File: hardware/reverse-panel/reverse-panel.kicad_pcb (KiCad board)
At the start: 2 copper layers, 116 x 102 mm, 328 parts, among them J1 Conn_01x03, U1 WCH CH32V003F4U6

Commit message: cleanup fab files
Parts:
- removed the R2 at (32.4, 50.0)
- removed the R2 at (84.4, 50.0)
- removed the R2 at (84.4, 102.0)
- removed the R2 at (32.4, 102.0)
- removed the R7 at (67.6, 50.0)
- removed the R7 at (119.6, 102.0)
- removed the R7 at (67.6, 102.0)
- removed the R7 at (119.6, 50.0)
- removed the align-r1 at (27.8, 104.4)
- removed the align-r1 at (79.8, 52.4)
- removed the align-r1 at (27.8, 52.4)
- removed the align-r1 at (79.8, 104.4)
- added R2: 47R, Resistor_SMD:R_0402_1005Metric, F.Cu at (84.4, 58.4)
- added R2: 47R, Resistor_SMD:R_0402_1005Metric, F.Cu at (32.4, 58.4)
- added R2: 47R, Resistor_SMD:R_0402_1005Metric, F.Cu at (32.4, 110.4)
- added R2: 47R, Resistor_SMD:R_0402_1005Metric, F.Cu at (84.4, 110.4)
- added R7: 47R, Resistor_SMD:R_0402_1005Metric, F.Cu at (67.6, 58.4)
- added R7: 47R, Resistor_SMD:R_0402_1005Metric, F.Cu at (119.6, 110.4)
- added R7: 47R, Resistor_SMD:R_0402_1005Metric, F.Cu at (119.6, 58.4)
- added R7: 47R, Resistor_SMD:R_0402_1005Metric, F.Cu at (67.6, 110.4)
- added align-r1: , , F.Cu at (79.8, 47.3)
- added align-r1: , , F.Cu at (79.8, 99.3)
- added align-r1: , , F.Cu at (27.8, 47.3)
- added align-r1: , , F.Cu at (27.8, 99.3)
- added align-r3: , , F.Cu at (27.8, 52.4)
- added align-r3: , , F.Cu at (79.8, 104.4)
- added align-r3: , , F.Cu at (27.8, 104.4)
- added align-r3: , , F.Cu at (79.8, 52.4)
- added align-r4: , , F.Cu at (72.2, 104.4)
- added align-r4: , , F.Cu at (124.2, 52.4)
- added align-r4: , , F.Cu at (72.2, 52.4)
- added align-r4: , , F.Cu at (124.2, 104.4)
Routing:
- net GND: track 17.1 -> 75.8 mm, vias 476 -> 424
- net /touch2: track 34.8 -> 66.6 mm
- net GP7: track 154.5 -> 139.2 mm
- net PWM2: track 65.3 -> 79.1 mm
- net PWM7: track 66.1 -> 80.0 mm
- net GP2: track 153.2 -> 140.5 mm
- net /touch1: track 68.9 -> 71.7 mm, vias 4 -> 12
- net Net-(D3-A): track 53.8 -> 52.0 mm
- net Net-(D13-A): track 53.2 -> 52.0 mm
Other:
- board size 116 x 102 mm -> 116.1 x 102.1 mm
- board text removed: "import QR SVG scale 0.2"

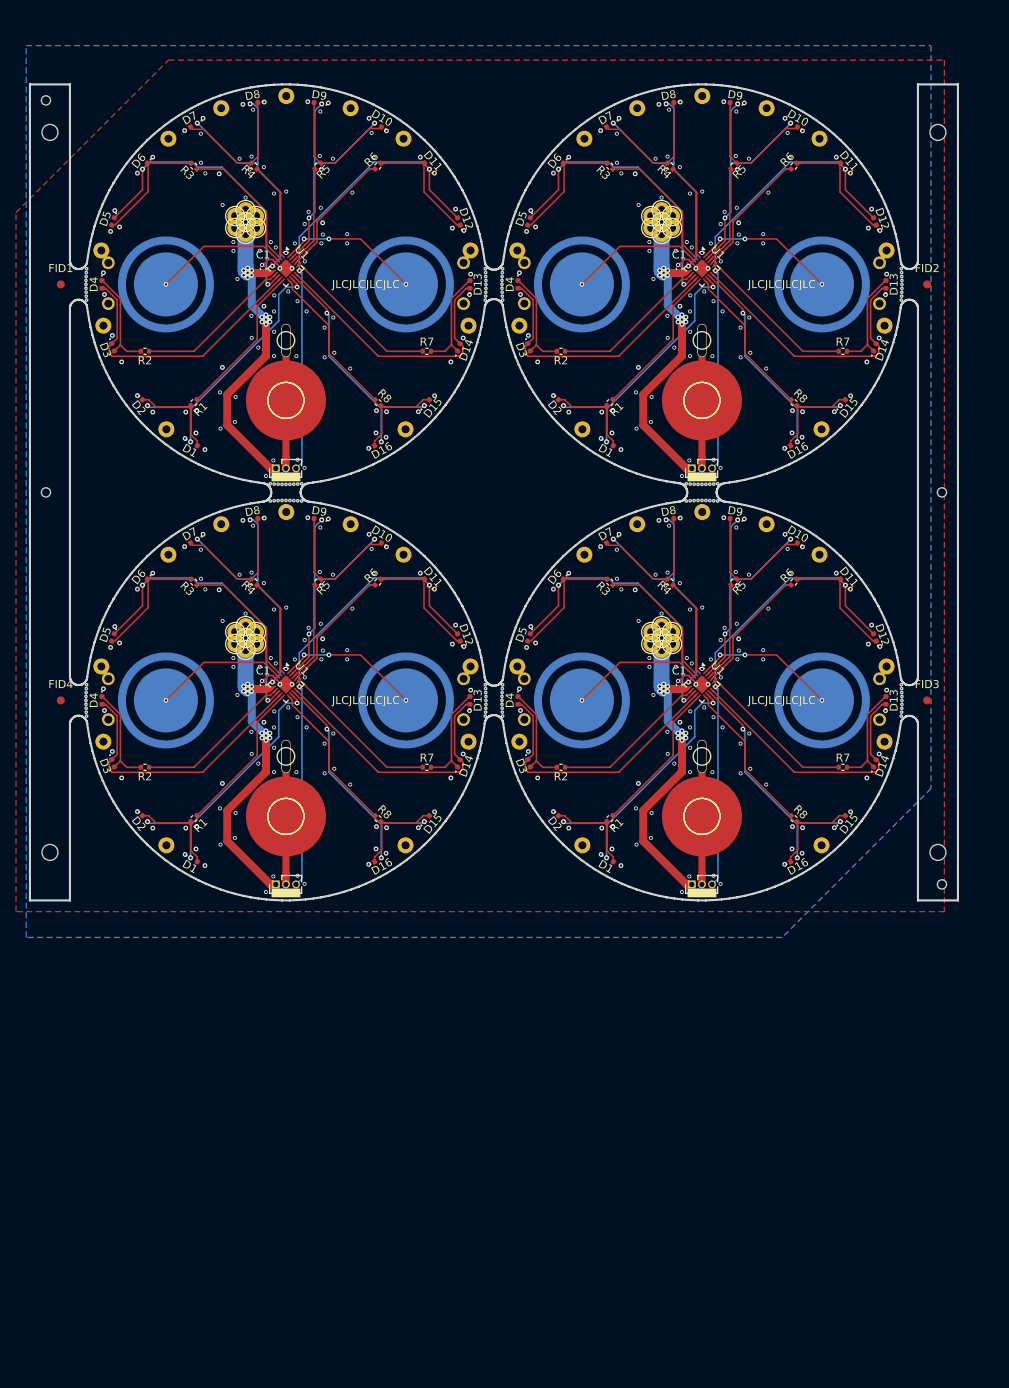
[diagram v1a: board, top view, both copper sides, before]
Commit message: rebuild panel with all SWD ports toward outside
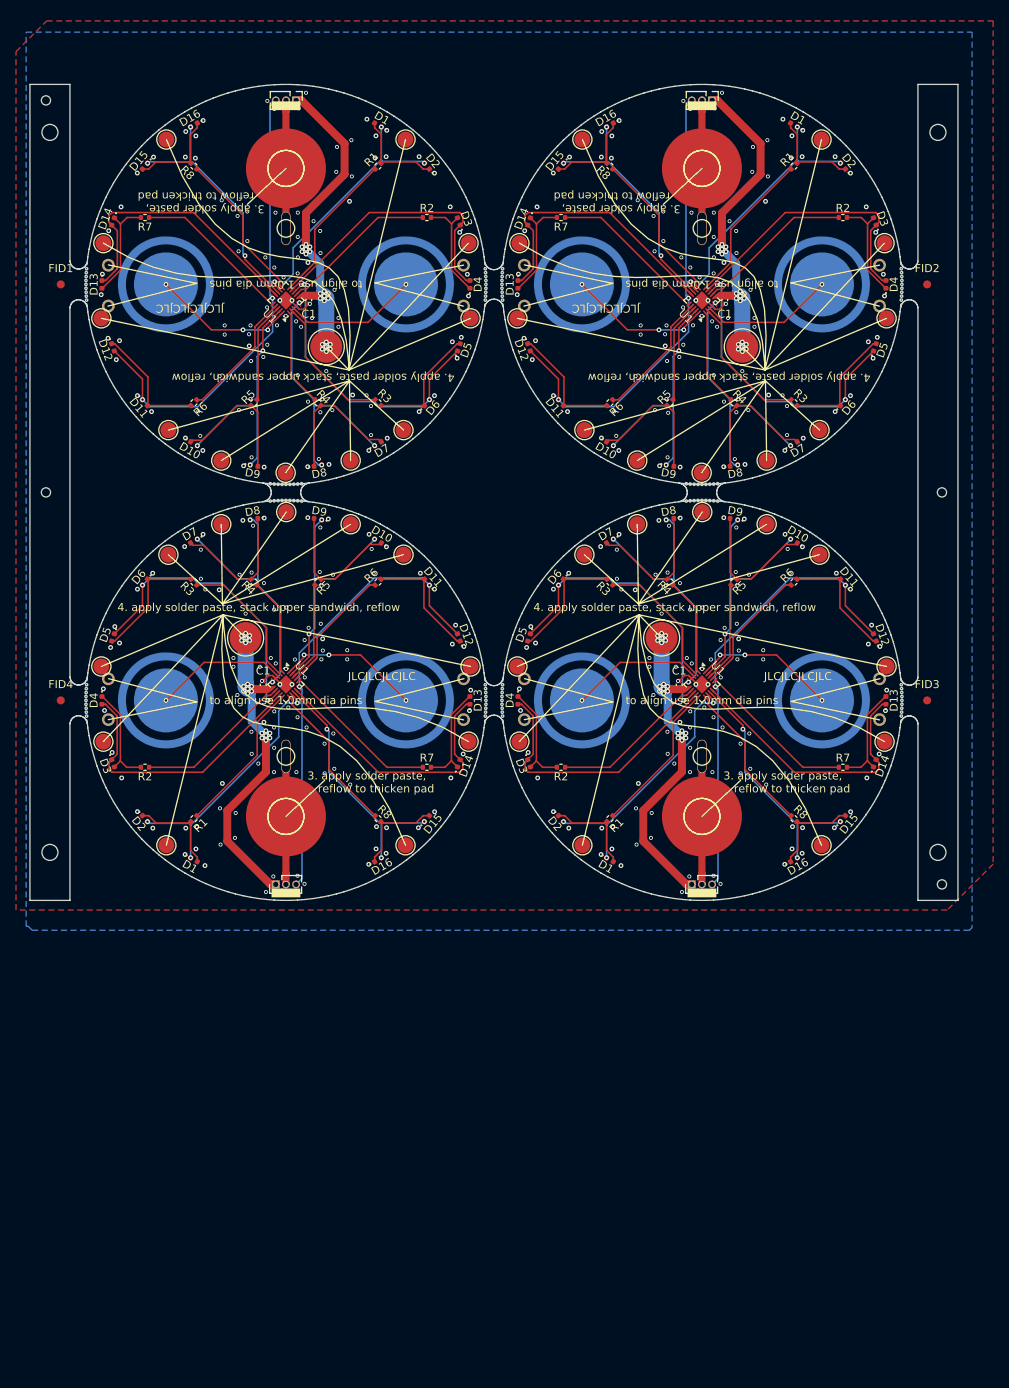
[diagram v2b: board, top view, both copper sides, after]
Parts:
- removed the - at (50.0, 64.5)
- removed the - at (102.0, 64.5)
- removed the B1 at (50.0, 64.5)
- removed the B1 at (102.0, 64.5)
- removed the C1 at (47.1, 48.0)
- removed the C1 at (99.2, 48.0)
- removed the D1 at (38.5, 69.9)
- removed the D1 at (90.5, 69.9)
- removed the D10 at (113.5, 30.1)
- removed the D10 at (61.5, 30.1)
- removed the D11 at (119.6, 35.2)
- removed the D11 at (67.6, 35.2)
- removed the D12 at (123.6, 42.1)
- removed the D12 at (71.6, 42.1)
- removed the D13 at (73.0, 50.0)
- removed the D13 at (125.0, 50.0)
- removed the D14 at (71.6, 57.9)
- removed the D14 at (123.6, 57.9)
- removed the D15 at (67.6, 64.8)
- removed the D15 at (119.6, 64.8)
- removed the D16 at (61.5, 69.9)
- removed the D16 at (113.5, 69.9)
- removed the D2 at (32.4, 64.8)
- removed the D2 at (84.4, 64.8)
- removed the D3 at (80.4, 57.9)
- removed the D3 at (28.4, 57.9)
- removed the D4 at (79.0, 50.0)
- removed the D4 at (27.0, 50.0)
- removed the D5 at (80.4, 42.1)
- removed the D5 at (28.4, 42.1)
- removed the D6 at (84.4, 35.2)
- removed the D6 at (32.4, 35.2)
- removed the D7 at (38.5, 30.1)
- removed the D7 at (90.5, 30.1)
- removed the D8 at (98.0, 27.3)
- removed the D8 at (46.0, 27.3)
- removed the D9 at (106.0, 27.3)
- removed the D9 at (54.0, 27.3)
- removed the J1 at (48.7, 73.0)
- removed the J1 at (100.7, 73.0)
- removed the R1 at (38.5, 64.8)
- removed the R1 at (90.5, 64.8)
- removed the R2 at (84.4, 58.4)
- removed the R2 at (32.4, 58.4)
- removed the R3 at (90.5, 35.2)
- removed the R3 at (38.5, 35.2)
- removed the R4 at (46.0, 35.2)
- removed the R4 at (98.0, 35.2)
- removed the R5 at (106.0, 35.2)
- removed the R5 at (54.0, 35.2)
- removed the R6 at (61.5, 35.2)
- removed the R6 at (113.5, 35.2)
- removed the R7 at (67.6, 58.4)
- removed the R7 at (119.6, 58.4)
- removed the R8 at (113.5, 64.8)
- removed the R8 at (61.5, 64.8)
- removed the S1 at (65.0, 50.0)
- removed the S1 at (117.0, 50.0)
- removed the S2 at (35.0, 50.0)
- removed the S2 at (87.0, 50.0)
- removed the U1 at (102.0, 48.0)
- removed the U1 at (50.0, 48.0)
- removed the align-r1 at (79.8, 47.3)
- removed the align-r1 at (27.8, 47.3)
- removed the align-r2 at (124.2, 47.3)
- removed the align-r2 at (72.2, 47.3)
- removed the align-r3 at (27.8, 52.4)
- removed the align-r3 at (79.8, 52.4)
- removed the align-r4 at (124.2, 52.4)
- removed the align-r4 at (72.2, 52.4)
- removed the battery-eject1 at (50.0, 57.0)
- removed the battery-eject1 at (102.0, 57.0)
- removed the stitch1 at (116.9, 120.1)
- removed the stitch1 at (41.9, 28.0)
- removed the stitch1 at (87.1, 120.1)
- removed the stitch1 at (110.1, 80.0)
- removed the stitch1 at (102.0, 78.5)
- removed the stitch1 at (72.8, 107.2)
- removed the stitch1 at (87.3, 83.8)
- removed the stitch1 at (35.1, 68.1)
- removed the stitch1 at (116.9, 68.1)
- removed the stitch1 at (125.1, 97.8)
- removed the stitch1 at (50.0, 78.5)
- removed the stitch1 at (64.7, 31.8)
- removed the stitch1 at (116.7, 31.8)
- removed the stitch1 at (87.1, 68.1)
- removed the stitch1 at (27.2, 107.2)
- removed the stitch1 at (64.9, 68.1)
- removed the stitch1 at (58.1, 28.0)
- removed the stitch1 at (124.8, 107.2)
- removed the stitch1 at (35.1, 120.1)
- removed the stitch1 at (102.0, 26.5)
- removed the stitch1 at (79.2, 55.2)
- removed the stitch1 at (35.3, 31.8)
- removed the stitch1 at (73.1, 45.8)
- removed the stitch1 at (41.9, 80.0)
- removed the stitch1 at (27.2, 55.2)
- removed the stitch1 at (78.9, 97.8)
- removed the stitch1 at (64.9, 120.1)
- removed the stitch1 at (93.9, 28.0)
- removed the stitch1 at (78.9, 45.8)
- removed the stitch1 at (26.9, 45.8)
- removed the stitch1 at (73.1, 97.8)
- removed the stitch1 at (87.3, 31.8)
- removed the stitch1 at (124.8, 55.2)
- removed the stitch1 at (125.1, 45.8)
- removed the stitch1 at (58.1, 80.0)
- removed the stitch1 at (93.9, 80.0)
- removed the stitch1 at (50.0, 26.5)
- removed the stitch1 at (26.9, 97.8)
- removed the stitch1 at (35.3, 83.8)
- removed the stitch1 at (64.7, 83.8)
- removed the stitch1 at (72.8, 55.2)
- removed the stitch1 at (116.7, 83.8)
- removed the stitch1 at (110.1, 28.0)
- removed the stitch1 at (79.2, 107.2)
- removed through-r1 (x4), through-r2 (x4), through-r3 (x4), through-r4 (x4), through-r5 (x4), through-r6 (x4), through-r7 (x4): TestPoint_THTPad_D2.0mm_Drill1.0mm, TestPoint:TestPoint_THTPad_D2.0mm_Drill1.0mm
- added -, B1: BAT-, TestPoint:TestPoint_Pad_D4.0mm, F.Cu at (50.0, 35.5)
- added -, B1: BAT-, TestPoint:TestPoint_Pad_D4.0mm, F.Cu at (102.0, 35.5)
- added C1: 1u, Capacitor_SMD:C_0402_1005Metric, F.Cu at (52.9, 52.0)
- added C1: 1u, Capacitor_SMD:C_0402_1005Metric, F.Cu at (104.8, 52.0)
- added D1: LED, LED_SMD:LED_0402_1005Metric, F.Cu at (61.5, 30.1)
- added D1: LED, LED_SMD:LED_0402_1005Metric, F.Cu at (113.5, 30.1)
- added D10: LED, LED_SMD:LED_0402_1005Metric, F.Cu at (38.5, 69.9)
- added D10: LED, LED_SMD:LED_0402_1005Metric, F.Cu at (90.5, 69.9)
- added D11: LED, LED_SMD:LED_0402_1005Metric, F.Cu at (32.4, 64.8)
- added D11: LED, LED_SMD:LED_0402_1005Metric, F.Cu at (84.4, 64.8)
- added D12: LED, LED_SMD:LED_0402_1005Metric, F.Cu at (80.4, 57.9)
- added D12: LED, LED_SMD:LED_0402_1005Metric, F.Cu at (28.4, 57.9)
- added D13: LED, LED_SMD:LED_0402_1005Metric, F.Cu at (79.0, 50.0)
- added D13: LED, LED_SMD:LED_0402_1005Metric, F.Cu at (27.0, 50.0)
- added D14: LED, LED_SMD:LED_0402_1005Metric, F.Cu at (80.4, 42.1)
- added D14: LED, LED_SMD:LED_0402_1005Metric, F.Cu at (28.4, 42.1)
- added D15: LED, LED_SMD:LED_0402_1005Metric, F.Cu at (84.4, 35.2)
- added D15: LED, LED_SMD:LED_0402_1005Metric, F.Cu at (32.4, 35.2)
- added D16: LED, LED_SMD:LED_0402_1005Metric, F.Cu at (90.5, 30.1)
- added D16: LED, LED_SMD:LED_0402_1005Metric, F.Cu at (38.5, 30.1)
- added D2: LED, LED_SMD:LED_0402_1005Metric, F.Cu at (67.6, 35.2)
- added D2: LED, LED_SMD:LED_0402_1005Metric, F.Cu at (119.6, 35.2)
- added D3: LED, LED_SMD:LED_0402_1005Metric, F.Cu at (71.6, 42.1)
- added D3: LED, LED_SMD:LED_0402_1005Metric, F.Cu at (123.6, 42.1)
- added D4: LED, LED_SMD:LED_0402_1005Metric, F.Cu at (125.0, 50.0)
- added D4: LED, LED_SMD:LED_0402_1005Metric, F.Cu at (73.0, 50.0)
- added D5: LED, LED_SMD:LED_0402_1005Metric, F.Cu at (123.6, 57.9)
- added D5: LED, LED_SMD:LED_0402_1005Metric, F.Cu at (71.6, 57.9)
- added D6: LED, LED_SMD:LED_0402_1005Metric, F.Cu at (119.6, 64.8)
- added D6: LED, LED_SMD:LED_0402_1005Metric, F.Cu at (67.6, 64.8)
- added D7: LED, LED_SMD:LED_0402_1005Metric, F.Cu at (113.5, 69.9)
- added D7: LED, LED_SMD:LED_0402_1005Metric, F.Cu at (61.5, 69.9)
- added D8: LED, LED_SMD:LED_0402_1005Metric, F.Cu at (54.0, 72.7)
- added D8: LED, LED_SMD:LED_0402_1005Metric, F.Cu at (106.0, 72.7)
- added D9: LED, LED_SMD:LED_0402_1005Metric, F.Cu at (46.0, 72.7)
- added D9: LED, LED_SMD:LED_0402_1005Metric, F.Cu at (98.0, 72.7)
- added J1: Conn_01x03, Connector_PinHeader_1.27mm:PinHeader_1x03_P1.27mm_Vertical, F.Cu at (103.3, 27.0)
- added J1: Conn_01x03, Connector_PinHeader_1.27mm:PinHeader_1x03_P1.27mm_Vertical, F.Cu at (51.3, 27.0)
- added R1: 47R, Resistor_SMD:R_0402_1005Metric, F.Cu at (113.5, 35.2)
- added R1: 47R, Resistor_SMD:R_0402_1005Metric, F.Cu at (61.5, 35.2)
- added R2: 47R, Resistor_SMD:R_0402_1005Metric, F.Cu at (67.6, 41.6)
- added R2: 47R, Resistor_SMD:R_0402_1005Metric, F.Cu at (119.6, 41.6)
- added R3: 47R, Resistor_SMD:R_0402_1005Metric, F.Cu at (113.5, 64.8)
- added R3: 47R, Resistor_SMD:R_0402_1005Metric, F.Cu at (61.5, 64.8)
- added R4: 47R, Resistor_SMD:R_0402_1005Metric, F.Cu at (106.0, 64.8)
- added R4: 47R, Resistor_SMD:R_0402_1005Metric, F.Cu at (54.0, 64.8)
- added R5: 47R, Resistor_SMD:R_0402_1005Metric, F.Cu at (98.0, 64.8)
- added R5: 47R, Resistor_SMD:R_0402_1005Metric, F.Cu at (46.0, 64.8)
- added R6: 47R, Resistor_SMD:R_0402_1005Metric, F.Cu at (90.5, 64.8)
- added R6: 47R, Resistor_SMD:R_0402_1005Metric, F.Cu at (38.5, 64.8)
- added R7: 47R, Resistor_SMD:R_0402_1005Metric, F.Cu at (32.4, 41.6)
- added R7: 47R, Resistor_SMD:R_0402_1005Metric, F.Cu at (84.4, 41.6)
- added R8: 47R, Resistor_SMD:R_0402_1005Metric, F.Cu at (38.5, 35.2)
- added R8: 47R, Resistor_SMD:R_0402_1005Metric, F.Cu at (90.5, 35.2)
- added S1: touch, TestPoint:TestPoint_Pad_D4.0mm, B.Cu at (35.0, 50.0)
- added S1: touch, TestPoint:TestPoint_Pad_D4.0mm, B.Cu at (87.0, 50.0)
- added S2: touch, TestPoint:TestPoint_Pad_D4.0mm, B.Cu at (117.0, 50.0)
- added S2: touch, TestPoint:TestPoint_Pad_D4.0mm, B.Cu at (65.0, 50.0)
- added U1: WCH CH32V003F4U6, Package_DFN_QFN:QFN-20-1EP_3x3mm_P0.4mm_EP1.65x1.65mm, F.Cu at (102.0, 52.0)
- added U1: WCH CH32V003F4U6, Package_DFN_QFN:QFN-20-1EP_3x3mm_P0.4mm_EP1.65x1.65mm, F.Cu at (50.0, 52.0)
- added align-r1: , , F.Cu at (72.2, 52.7)
- added align-r1: , , F.Cu at (124.2, 52.7)
- added align-r2: , , F.Cu at (79.8, 52.7)
- added align-r2: , , F.Cu at (27.8, 52.7)
- added align-r3: , , F.Cu at (72.2, 47.6)
- added align-r3: , , F.Cu at (124.2, 47.6)
- added align-r4: , , F.Cu at (27.8, 47.6)
- added align-r4: , , F.Cu at (79.8, 47.6)
- added battery-eject1: TestPoint_THTPad_3.0x3.0mm_Drill1.5mm, TestPoint:TestPoint_THTPad_3.0x3.0mm_Drill1.5mm, F.Cu at (102.0, 43.0)
- added battery-eject1: TestPoint_THTPad_3.0x3.0mm_Drill1.5mm, TestPoint:TestPoint_THTPad_3.0x3.0mm_Drill1.5mm, F.Cu at (50.0, 43.0)
- added contact-r1: TestPoint_Pad_D4.0mm, TestPoint:TestPoint_Pad_D4.0mm, F.Cu at (97.0, 94.2)
- added contact-r1: TestPoint_Pad_D4.0mm, TestPoint:TestPoint_Pad_D4.0mm, F.Cu at (107.0, 57.8)
- added contact-r1: TestPoint_Pad_D4.0mm, TestPoint:TestPoint_Pad_D4.0mm, F.Cu at (45.0, 94.2)
- added contact-r1: TestPoint_Pad_D4.0mm, TestPoint:TestPoint_Pad_D4.0mm, F.Cu at (55.0, 57.8)
- added stitch1: TestPoint_Pad_D2.0mm, TestPoint:TestPoint_Pad_D2.0mm, F.Cu at (50.0, 73.5)
- added stitch1: TestPoint_Pad_D2.0mm, TestPoint:TestPoint_Pad_D2.0mm, F.Cu at (58.1, 72.0)
- added stitch1: TestPoint_Pad_D2.0mm, TestPoint:TestPoint_Pad_D2.0mm, F.Cu at (27.2, 44.8)
- added stitch1: TestPoint_Pad_D2.0mm, TestPoint:TestPoint_Pad_D2.0mm, F.Cu at (26.9, 54.2)
- added stitch1: TestPoint_Pad_D2.0mm, TestPoint:TestPoint_Pad_D2.0mm, F.Cu at (41.9, 72.0)
- added stitch1: TestPoint_Pad_D2.0mm, TestPoint:TestPoint_Pad_D2.0mm, F.Cu at (87.1, 120.1)
- added stitch1: TestPoint_Pad_D2.0mm, TestPoint:TestPoint_Pad_D2.0mm, F.Cu at (79.2, 107.2)
- added stitch1: TestPoint_Pad_D2.0mm, TestPoint:TestPoint_Pad_D2.0mm, F.Cu at (110.1, 80.0)
- added stitch1: TestPoint_Pad_D2.0mm, TestPoint:TestPoint_Pad_D2.0mm, F.Cu at (64.7, 68.2)
- added stitch1: TestPoint_Pad_D2.0mm, TestPoint:TestPoint_Pad_D2.0mm, F.Cu at (73.1, 54.2)
- added stitch1: TestPoint_Pad_D2.0mm, TestPoint:TestPoint_Pad_D2.0mm, F.Cu at (124.8, 44.8)
- added stitch1: TestPoint_Pad_D2.0mm, TestPoint:TestPoint_Pad_D2.0mm, F.Cu at (78.9, 54.2)
- added stitch1: TestPoint_Pad_D2.0mm, TestPoint:TestPoint_Pad_D2.0mm, F.Cu at (41.9, 80.0)
- added stitch1: TestPoint_Pad_D2.0mm, TestPoint:TestPoint_Pad_D2.0mm, F.Cu at (73.1, 97.8)
- added stitch1: TestPoint_Pad_D2.0mm, TestPoint:TestPoint_Pad_D2.0mm, F.Cu at (102.0, 78.5)
- added stitch1: TestPoint_Pad_D2.0mm, TestPoint:TestPoint_Pad_D2.0mm, F.Cu at (102.0, 73.5)
- added stitch1: TestPoint_Pad_D2.0mm, TestPoint:TestPoint_Pad_D2.0mm, F.Cu at (78.9, 97.8)
- added stitch1: TestPoint_Pad_D2.0mm, TestPoint:TestPoint_Pad_D2.0mm, F.Cu at (35.3, 83.8)
- added stitch1: TestPoint_Pad_D2.0mm, TestPoint:TestPoint_Pad_D2.0mm, F.Cu at (35.1, 31.9)
- added stitch1: TestPoint_Pad_D2.0mm, TestPoint:TestPoint_Pad_D2.0mm, F.Cu at (72.8, 107.2)
- added stitch1: TestPoint_Pad_D2.0mm, TestPoint:TestPoint_Pad_D2.0mm, F.Cu at (26.9, 97.8)
- added stitch1: TestPoint_Pad_D2.0mm, TestPoint:TestPoint_Pad_D2.0mm, F.Cu at (58.1, 80.0)
- added stitch1: TestPoint_Pad_D2.0mm, TestPoint:TestPoint_Pad_D2.0mm, F.Cu at (87.3, 68.2)
- added stitch1: TestPoint_Pad_D2.0mm, TestPoint:TestPoint_Pad_D2.0mm, F.Cu at (79.2, 44.8)
- added stitch1: TestPoint_Pad_D2.0mm, TestPoint:TestPoint_Pad_D2.0mm, F.Cu at (116.9, 31.9)
- added stitch1: TestPoint_Pad_D2.0mm, TestPoint:TestPoint_Pad_D2.0mm, F.Cu at (110.1, 72.0)
- added stitch1: TestPoint_Pad_D2.0mm, TestPoint:TestPoint_Pad_D2.0mm, F.Cu at (116.7, 83.8)
- added stitch1: TestPoint_Pad_D2.0mm, TestPoint:TestPoint_Pad_D2.0mm, F.Cu at (93.9, 72.0)
- added stitch1: TestPoint_Pad_D2.0mm, TestPoint:TestPoint_Pad_D2.0mm, F.Cu at (72.8, 44.8)
- added stitch1: TestPoint_Pad_D2.0mm, TestPoint:TestPoint_Pad_D2.0mm, F.Cu at (93.9, 80.0)
- added stitch1: TestPoint_Pad_D2.0mm, TestPoint:TestPoint_Pad_D2.0mm, F.Cu at (35.3, 68.2)
- added stitch1: TestPoint_Pad_D2.0mm, TestPoint:TestPoint_Pad_D2.0mm, F.Cu at (64.9, 31.9)
- added stitch1: TestPoint_Pad_D2.0mm, TestPoint:TestPoint_Pad_D2.0mm, F.Cu at (116.7, 68.2)
- added stitch1: TestPoint_Pad_D2.0mm, TestPoint:TestPoint_Pad_D2.0mm, F.Cu at (124.8, 107.2)
- added stitch1: TestPoint_Pad_D2.0mm, TestPoint:TestPoint_Pad_D2.0mm, F.Cu at (87.1, 31.9)
- added stitch1: TestPoint_Pad_D2.0mm, TestPoint:TestPoint_Pad_D2.0mm, F.Cu at (125.1, 97.8)
- added stitch1: TestPoint_Pad_D2.0mm, TestPoint:TestPoint_Pad_D2.0mm, F.Cu at (64.7, 83.8)
- added stitch1: TestPoint_Pad_D2.0mm, TestPoint:TestPoint_Pad_D2.0mm, F.Cu at (27.2, 107.2)
- added stitch1: TestPoint_Pad_D2.0mm, TestPoint:TestPoint_Pad_D2.0mm, F.Cu at (116.9, 120.1)
- added stitch1: TestPoint_Pad_D2.0mm, TestPoint:TestPoint_Pad_D2.0mm, F.Cu at (87.3, 83.8)
- added stitch1: TestPoint_Pad_D2.0mm, TestPoint:TestPoint_Pad_D2.0mm, F.Cu at (35.1, 120.1)
- added stitch1: TestPoint_Pad_D2.0mm, TestPoint:TestPoint_Pad_D2.0mm, F.Cu at (125.1, 54.2)
- added stitch1: TestPoint_Pad_D2.0mm, TestPoint:TestPoint_Pad_D2.0mm, F.Cu at (64.9, 120.1)
- added stitch1: TestPoint_Pad_D2.0mm, TestPoint:TestPoint_Pad_D2.0mm, F.Cu at (50.0, 78.5)
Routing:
- net GND: vias 424 -> 420
- net +3V0: vias 56 -> 84
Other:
- board size 116.1 x 102.1 mm -> 116 x 102 mm
- board text added: "3. apply solder paste, reflow to thicken pad"
- board text added: "4. apply solder paste, stack upper sandwich, reflow"
- board text added: "jlcpcb.com/help/article/How-to-remove-order-number-from-your-PCB jlcpcb.com/help/article/Panelizing-your-PCB-for-Assembly jlcpcb.com/help/article/How-to-add-tooling-holes-for-PCB-assembly-order"
- board text added: "to align use 1.0mm dia pins"
- board text removed: "github.com/eutectic6337/coin1"
